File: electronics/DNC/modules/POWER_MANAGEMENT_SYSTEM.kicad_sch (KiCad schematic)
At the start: 35 parts, among them U1 INA169

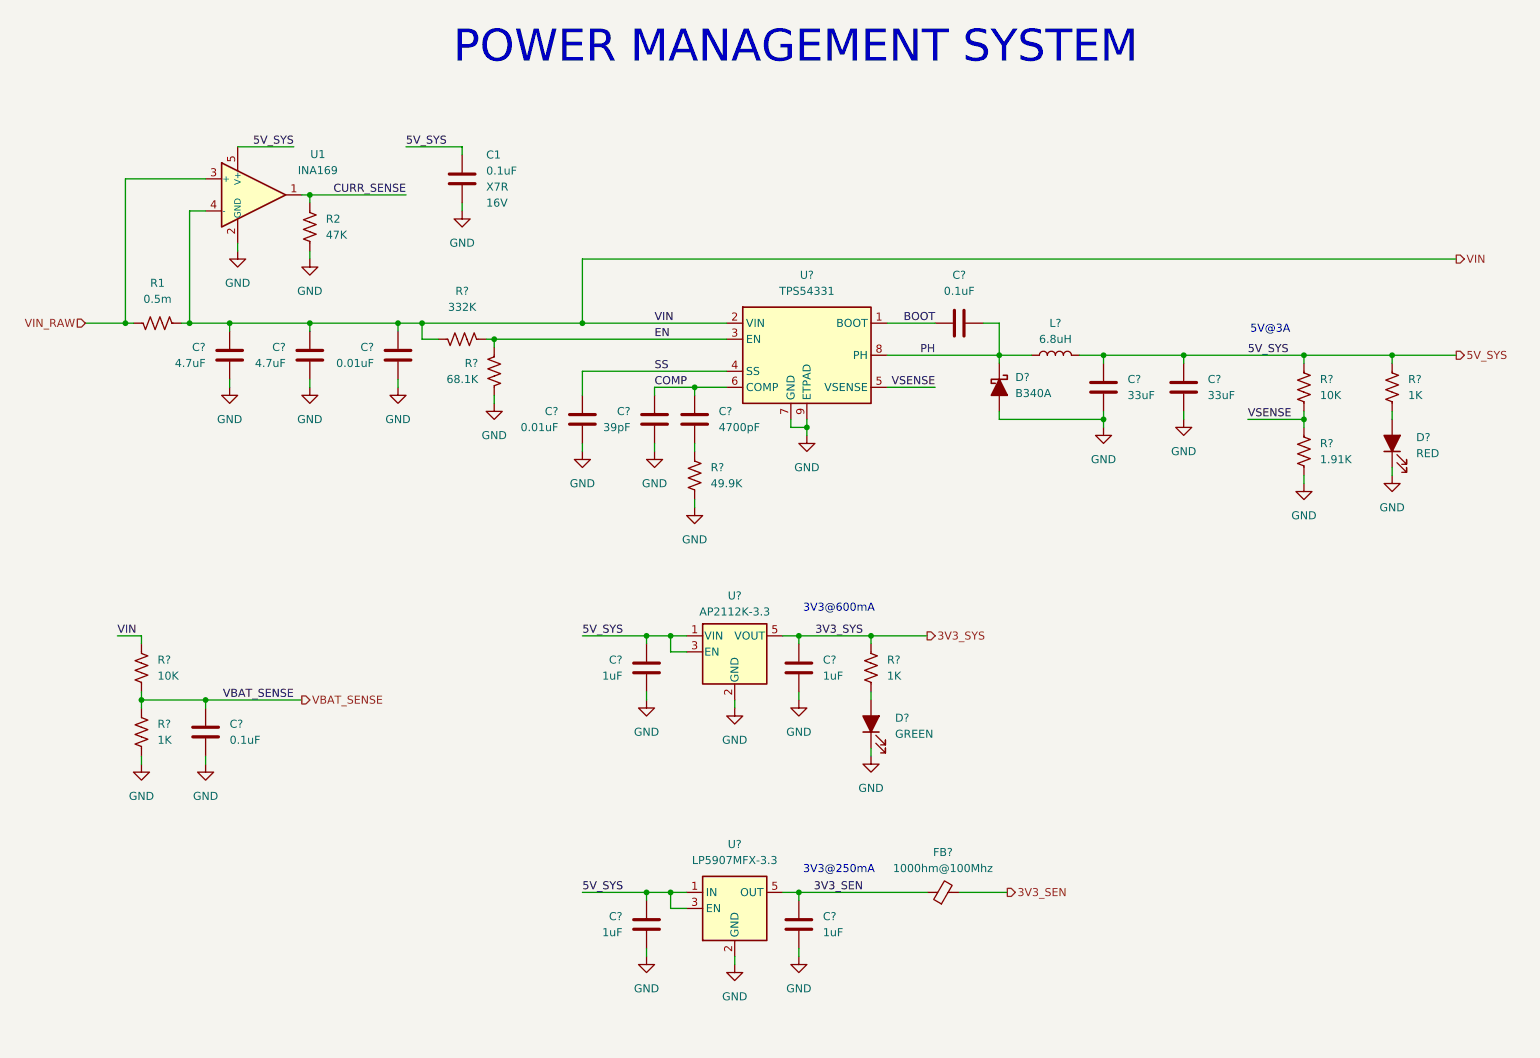
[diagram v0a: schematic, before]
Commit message: Se reemplazó la hoja del IMU por la de sensores y se agregó la hoja de indicadores
- Nueva hoja Sensores: IMU BMI270 (SPI1) y barómetro BMP581 (I2C1 propio, jumper BARO_ADDR).
- Nueva hoja Indicadores: buzzer piezo CPT-12123 con FDV303N y LEDs de estado en PB4/PB5.
- Se eliminó la hoja IMU.
- MicroSD por SDIO de 4 bits con filtro TPD6F002 y TVS ESD5Z3.3 en VDD.
- PMS: AP2112K en 3V3_SYS y LP5907 + ferrita en 3V3_SEN.
- Motores movidos a PA0-PA3 (TIM5) para liberar el SDIO.
- Arquitectura.drawio actualizado a la arquitectura v1 (ELRS por UART, sin OLED).
- Se agregó docs/RESUMEN_PROYECTO_DNC.md con decisiones y pendientes.

Co-Authored-By: Claude Opus 5.5 <noreply@anthropic.com>
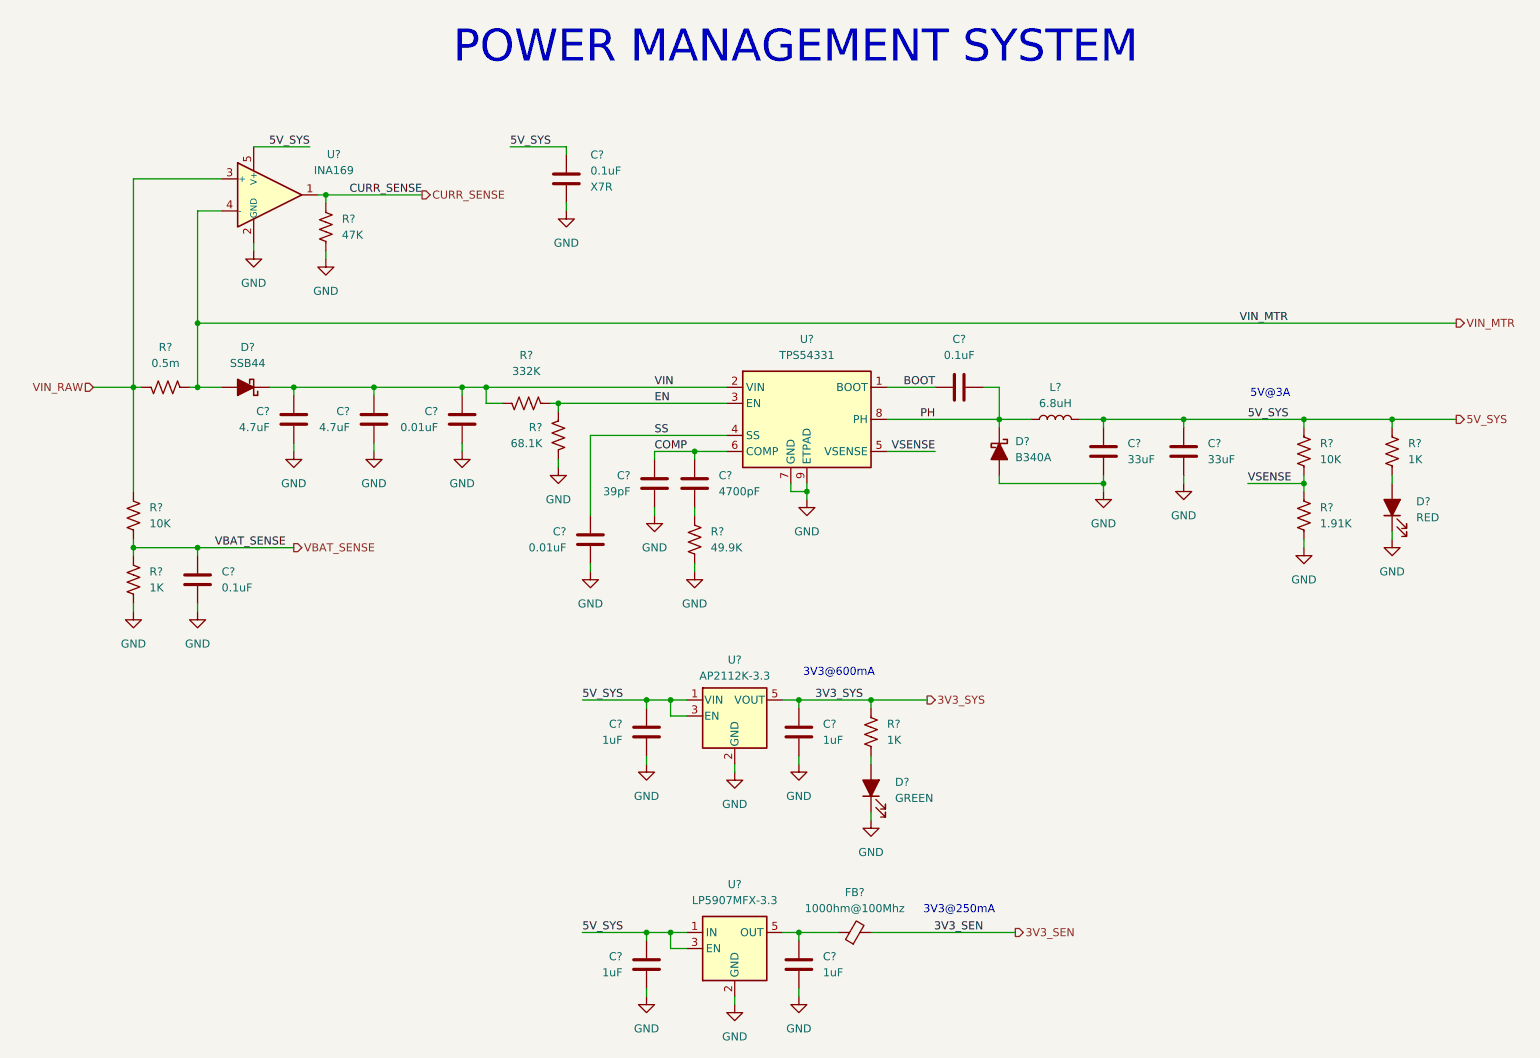
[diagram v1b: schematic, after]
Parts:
- added D?: SSB44, symbol Device:D_Schottky_Filled
- C?: renamed from C1; VOLTAGE 16V -> (none)
- renumbered R2 to R?, R1 to R?, U1 to U?
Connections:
- net 3V3_SEN: no longer C?.1, FB?.1, U?.5 (OUT)
- net VIN: now also D?.1 (K); no longer R?.1, R?.1, U?.4 (-)
- net VIN_RAW: now also R?.1
- new net: C?.1, FB?.1, U?.5 (OUT)
- new net VIN_MTR: D?.2 (A), R?.1, U?.4 (-)
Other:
- moved on the sheet: C?, D?, FB?, L?, R?, U?

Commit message: Se enlazó el TPS54331 a la librería SJ (SJ_Power:TPS54331DDA)
- PMS: el TPS54331 pasa de DC-DC_Converter (own_symbols) a SJ_Power:TPS54331DDA.
  Netlist verificado: todas las redes iguales; el pad térmico (pin 9, ahora PAD) sigue en GND.
- Indicadores y raíz: cambios menores de KiCad (referencias sin anotar).

Co-Authored-By: Claude Opus 5.5 <noreply@anthropic.com>
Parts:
- removed U?: TPS54331, Package_SO:TI_SO-PowerPAD-8_ThermalVias, symbol DC-DC_Converter:TPS54331
- added U?: TPS54331, Package_SO:TI_SO-PowerPAD-8_ThermalVias, symbol SJ_Power:TPS54331DDA
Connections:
- net BOOT: now also U?.1 (BOOT)
- net COMP: now also U?.6 (COMP)
- net EN: now also U?.3 (EN)
- net GND: now also U?.7 (GND), U?.9 (PAD)
- net PH: now also U?.8 (PH)
- net SS: now also U?.4 (SS)
- net VIN: now also U?.2 (VIN)
- net VSENSE: now also U?.5 (VSENSE)
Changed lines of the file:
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@@
+	)
+	(symbol
+		(lib_id "SJ_Power:TPS54331DDA")
+		(at 151.13 81.28 0)
+		(unit 1)
+		(body_style 1)
+		(exclude_from_sim no)
+		(in_bom yes)
+		(on_board yes)
+		(in_pos_files yes)
+		(dnp no)
+		(fields_autoplaced yes)
+		(property "Reference" "U?"
+			(at 151.13 68.58 0)
+			(show_name no)
+			(do_not_autoplace no)
+			(effects
+				(font
+					(size 1.27 1.27)
+				)
+			)
+		)
+		(property "Value" "TPS54331"
+			(at 151.13 71.12 0)
+			(show_name no)
+			(do_not_autoplace no)
+			(effects
+				(font
+					(size 1.27 1.27)
+				)
+			)
+		)
+		(property "Footprint" "Package_SO:TI_SO-PowerPAD-8_ThermalVias"
+			(at 173.99 90.17 0)
+			(hide yes)
+			(show_name no)
+			(do_not_autoplace no)
+			(effects
+				(font
+					(size 1.27 1.27)
+				)
+			)
+		)
+		(property "Datasheet" "https://www.ti.com/lit/ds/symlink/tps54331.pdf"
+			(at 176.53 92.71 0)
+			(hide yes)
+			(show_name no)
+			(do_not_autoplace no)
+			(effects
+				(font
+					(size 1.27 1.27)
+				)
+			)
+		)
+		(property "Description" "3.5V to 28V Input, 3A, 570kHz Step-Down Converter, SO PowerPAD-8 (DDA)"
+			(at 151.13 81.28 0)
+			(hide yes)
+			(show_name no)
+			(do_not_autoplace no)
+			(effects
+				(font
+					(size 1.27 1.27)
+				)
+			)
+		)
+		(property "Manufacturer" ""
+			(at 151.13 81.28 0)
+			(hide yes)
+			(show_name no)
+			(do_not_autoplace no)
+			(effects
+				(font
+					(size 1.27 1.27)
+				)
+			)
+		)
+		(property "Mfg Part #" ""
+			(at 151.13 81.28 0)
+			(hide yes)
+			(show_name no)
+			(do_not_autoplace no)
+			(effects
+				(font
+					(size 1.27 1.27)
+				)
+			)
+		)
+		(property "LCSC Part #" ""
+			(at 151.13 81.28 0)
+			(hide yes)
+			(show_name no)
+			(do_not_autoplace no)
+			(effects
+				(font
+					(size 1.27 1.27)
+				)
+			)
+		)
+		(property "Supplier" ""
+			(at 151.13 81.28 0)
+			(hide yes)
+			(show_name no)
+			(do_not_autoplace no)
+			(effects
+				(font
+					(size 1.27 1.27)
+				)
+			)
+		)
+		(property "Cost" ""
+			(at 151.13 81.28 0)
+			(hide yes)
+			(show_name no)
+			(do_not_autoplace no)
+			(effects
+				(font
+					(size 1.27 1.27)
+				)
+			)
+		)
+		(property "Voltage" ""
+			(at 151.13 81.28 0)
+			(hide yes)
+			(show_name no)
+			(do_not_autoplace no)
+			(effects
+				(font
+					(size 1.27 1.27)
+				)
+			)
+		)
+		(property "Current" ""
+			(at 151.13 81.28 0)
+			(hide yes)
+			(show_name no)
+			(do_not_autoplace no)
+			(effects
+				(font
+					(size 1.27 1.27)
+				)
+			)
+		)
+		(property "TC" ""
+			(at 151.13 81.28 0)
+			(hide yes)
+			(show_name no)
+			(do_not_autoplace no)
+			(effects
+				(font
+					(size 1.27 1.27)
+				)
+			)
+		)
+		(property "Power" ""
+			(at 151.13 81.28 0)
+			(hide yes)
+			(show_name no)
+			(do_not_autoplace no)
+			(effects
+				(font
+					(size 1.27 1.27)
+				)
+			)
+		)
+		(property "Tol" ""
+			(at 151.13 81.28 0)
+			(hide yes)
+			(show_name no)
+			(do_not_autoplace no)
+			(effects
+				(font
+					(size 1.27 1.27)
+				)
+			)
+		)
+		(pin "7"
+		)
+		(pin "2"
+		)
+		(pin "5"
+		)
+		(pin "8"
+		)
+		(pin "4"
+		)
+		(pin "9"
+		)
+		(pin "6"
+		)
+		(pin "1"
+		)
+		(pin "3"
+		)
+		(instances
+			(project "DNC"
+				(path "/abee636e-ad3a-4ba4-b95f-d0cf4a6d3d85/df8dd51f-1e12-498a-8bd1-b79cac3ffc30"
+					(reference "U?")
+					(unit 1)
+				)
+			)
+		)
 	)
 	(symbol
@@
 					(unit 1)
 				)
-			)
-		)
-	)
-	(symbol
-		(lib_id "DC-DC_Converter:TPS54331")
-		(at 151.13 81.28 0)
-		(unit 1)
-		(body_style 1)
-		(exclude_from_sim no)
-		(in_bom yes)
-		(on_board yes)
-		(in_pos_files yes)
-		(dnp no)
-		(fields_autoplaced yes)
-		(property "Reference" "U?"
-			(at 151.13 68.58 0)
-			(show_name no)
-			(do_not_autoplace no)
-			(effects
-				(font
-					(size 1.27 1.27)
-				)
-			)
-		)
-		(property "Value" "TPS54331"
-			(at 151.13 71.12 0)
-			(show_name no)
-			(do_not_autoplace no)
-			(effects
-				(font
-					(size 1.27 1.27)
-				)
-			)
-		)
-		(property "Footprint" "Package_SO:TI_SO-PowerPAD-8_ThermalVias"
-			(at 173.99 90.17 0)
-			(hide yes)
-			(show_name no)
-			(do_not_autoplace no)
-			(effects
-				(font
-					(size 1.27 1.27)
-				)
-			)
-		)
-		(property "Datasheet" "https://www.ti.com/lit/ds/symlink/tps54331.pdf"
-			(at 176.53 92.71 0)
-			(hide yes)
-			(show_name no)
-			(do_not_autoplace no)
-			(effects
-				(font
-					(size 1.27 1.27)
-				)
-			)
-		)
-		(property "Description" "3.5V to 28V Input, 3A, Synchronous Step-Down Converter"
-			(at 151.13 81.28 0)
-			(hide yes)
-			(show_name no)
-			(do_not_autoplace no)
-			(effects
-				(font
-					(size 1.27 1.27)
-				)
-			)
-		)
-		(property "Manufacturer" ""
-			(at 151.13 81.28 0)
-			(hide yes)
-			(show_name no)
-			(do_not_autoplace no)
-			(effects
-				(font
-					(size 1.27 1.27)
-				)
-			)
-		)
-		(property "Mfg Part #" ""
-			(at 151.13 81.28 0)
-			(hide yes)
-			(show_name no)
-			(do_not_autoplace no)
-			(effects
-				(font
-					(size 1.27 1.27)
-				)
-			)
-		)
-		(property "LCSC Part #" ""
-			(at 151.13 81.28 0)
-			(hide yes)
-			(show_name no)
-			(do_not_autoplace no)
-			(effects
-				(font
-					(size 1.27 1.27)
-				)
-			)
-		)
-		(property "Supplier" ""
-			(at 151.13 81.28 0)
-			(hide yes)
-			(show_name no)
-			(do_not_autoplace no)
-			(effects
-				(font
-					(size 1.27 1.27)
-				)
-			)
-		)
-		(property "Cost" ""
-			(at 151.13 81.28 0)
-			(hide yes)
-			(show_name no)
-			(do_not_autoplace no)
-			(effects
-				(font
-					(size 1.27 1.27)
-				)
-			)
-		)
-		(property "Voltage" ""
-			(at 151.13 81.28 0)
-			(show_name no)
-			(do_not_autoplace no)
-			(effects
-				(font
-					(size 1.27 1.27)
-				)
-			)
-		)
-		(property "Current" ""
-			(at 151.13 81.28 0)
-			(show_name no)
-			(do_not_autoplace no)
-			(effects
-				(font
-					(size 1.27 1.27)
-				)
-			)
-		)
-		(property "TC" ""
-			(at 151.13 81.28 0)
-			(show_name no)
-			(do_not_autoplace no)
-			(effects
-				(font
-					(size 1.27 1.27)
-				)
-			)
-		)
-		(property "Power" ""
-			(at 151.13 81.28 0)
-			(show_name no)
-			(do_not_autoplace no)
-			(effects
-				(font
-					(size 1.27 1.27)
-				)
-			)
-		)
-		(property "Tol" ""
-			(at 151.13 81.28 0)
-			(show_name no)
-			(do_not_autoplace no)
-			(effects
-				(font
-					(size 1.27 1.27)
-				)
-			)
-		)
-		(pin "5"
-		)
-		(pin "2"
-		)
-		(pin "4"
-		)
-		(pin "7"
-		)
-		(pin "1"
-		)
-		(pin "6"
-		)
-		(pin "3"
-		)
-		(pin "9"
-		)
-		(pin "8"
-		)
-		(instances
-			(project "DNC"
-				(path "/abee636e-ad3a-4ba4-b95f-d0cf4a6d3d85/df8dd51f-1e12-498a-8bd1-b79cac3ffc30"
-					(reference "U?")
-					(unit 1)
-				)

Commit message: Buck TPS62162 en 3V3_SYS, secuencia de 3V3_SEN por PG y PWR_FLAG en el PMS
- 3V3_SYS: el AP2112K (LDO, ~0.5 W en SOT-23-5) se reemplaza por el buck síncrono
  TPS62162DSG (salida fija de 3.3 V, entrada de 3-17 V, 1 A). Símbolo y huella estándar de KiCad.
  Circuito según el datasheet SLVSAM2E: C_IN 10 uF, L 2.2 uH, C_OUT 22 uF, VOS en la salida,
  FB/AGND/PGND/pad a GND, EN a 5V_SYS.
- Secuencia: PG (drenador abierto, pull-up de 100 k a 3V3_SYS) -> EN del LP5907, así 3V3_SEN
  solo arranca con 3V3_SYS ya en regulación (VIH del LP5907 = 1.2 V; EN ~3.0 V con el
  pull-down interno de 1 M).
- PWR_FLAG en 5V_SYS, 3V3_SEN, entrada del TPS54331 (/PMS/VIN) y salida: el ERC del PMS y de
  Sensores queda sin avisos.

Co-Authored-By: Claude Opus 5.5 <noreply@anthropic.com>
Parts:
- removed C? (x2): 1uF, symbol Device:C
- removed D?: GREEN, symbol Device:LED_Filled
- removed R?: 1K, symbol Device:R_US
- removed U?: AP2112K-3.3, Package_TO_SOT_SMD:SOT-23-5, symbol Regulator_Linear:AP2112K-3.3
- added C?: 22uF, symbol Device:C
- added C?: 10uF, symbol Device:C
- added D?: GREEN, symbol Device:LED_Filled
- added L?: 2.2uH, symbol Device:L
- added R?: 1K, symbol Device:R_US
- added R?: 100K, symbol Device:R_US
- added U?: TPS62162DSG, Package_SON:Texas_DSG0008A_WSON-8-1EP_2x2mm_P0.5mm_EP0.9x1.6mm_ThermalVias, symbol Regulator_Switching:TPS62162DSG
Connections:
- net 3V3_SYS: now also C?.1, L?.2, R?.1, R?.1, U?.6 (VOS)
- net 5V_SYS: now also C?.1, U?.2 (VIN), U?.3 (EN); no longer U?.3 (EN)
- net GND: now also C?.2, C?.2, D?.1 (K), U?.1 (PGND), U?.4 (AGND), U?.5 (FB), U?.9 (PAD)
- new net: L?.1, U?.7 (SW)
- new net: D?.2 (A), R?.2
- new net PG: R?.2, U?.3 (EN), U?.8 (PG)
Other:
- note added: "3V3@1A"
- note removed: "3V3@600mA"
- moved on the sheet: C?

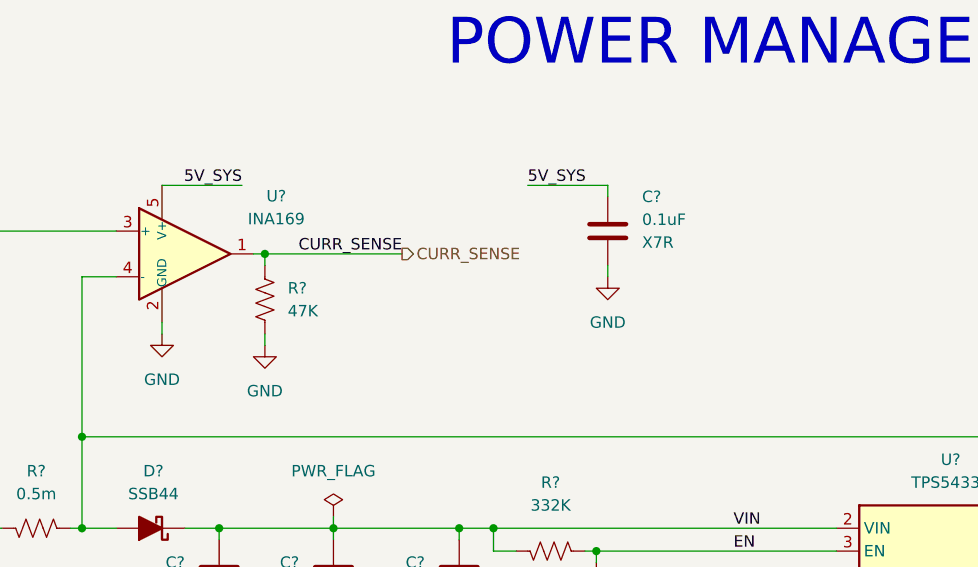
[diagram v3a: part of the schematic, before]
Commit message: Protección de entrada para 4S: TVS SMBJ18A e INA169 alimentado desde 3V3_SYS
- TVS: SMBJ26CA bidireccional (clamp ~42 V) -> SMBJ18A unidireccional (VR 18 V,
  VC 29.2 V @ 20.5 A), por debajo del máximo absoluto de 30 V del TPS54331. Símbolo
  genérico Diode:SM6T18A (misma geometría y familia de 600 W/SMB), huella Diode_SMD:D_SMB;
  cátodo a VIN_RAW.
- INA169: V+ y su desacoplo pasan de 5V_SYS a 3V3_SYS; la salida queda limitada a
  ~(V+ - 0.9 V), así que PB1 (ADC) no puede superar 3.3 V.
- RL 47k -> 27k: 13.5 mV/A, 1.89 V a 140 A (dentro de la salida garantizada). 10 nF en
  paralelo como filtro (~590 Hz).
- MVP1 = 4S. El 6S necesitaría un buck de 60 V; queda pospuesto.

Co-Authored-By: Claude Opus 5.5 <noreply@anthropic.com>
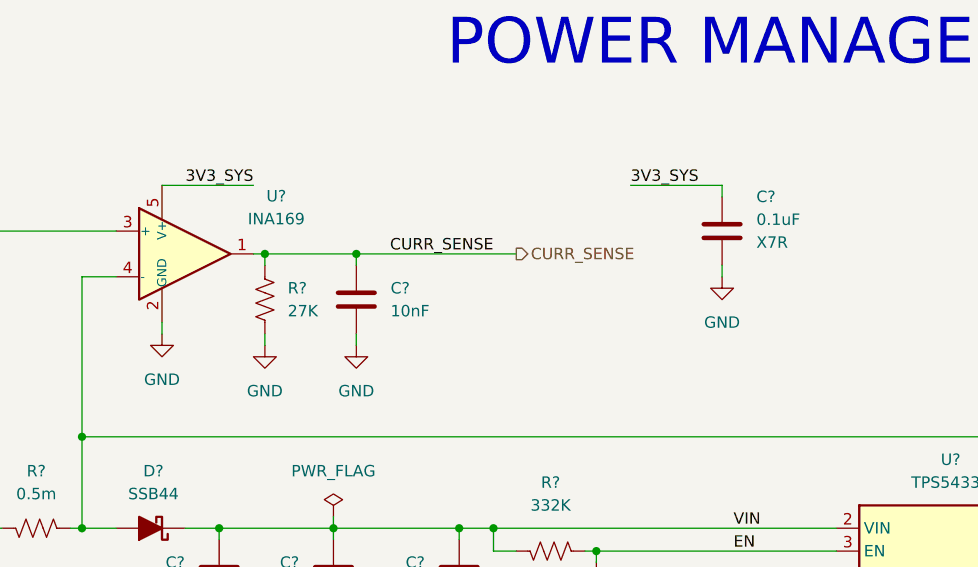
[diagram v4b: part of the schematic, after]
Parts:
- added C?: 10nF, symbol Device:C
- R?: value 47K -> 27K
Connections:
- net 3V3_SYS: now also C?.1, U?.5 (V+)
- net 5V_SYS: no longer C?.1, U?.5 (V+)
- net CURR_SENSE: now also C?.1
- net GND: now also C?.2
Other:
- moved on the sheet: C?
